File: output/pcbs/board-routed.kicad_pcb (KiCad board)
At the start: 2 copper layers, 141.8 x 108.1 mm, 41 parts

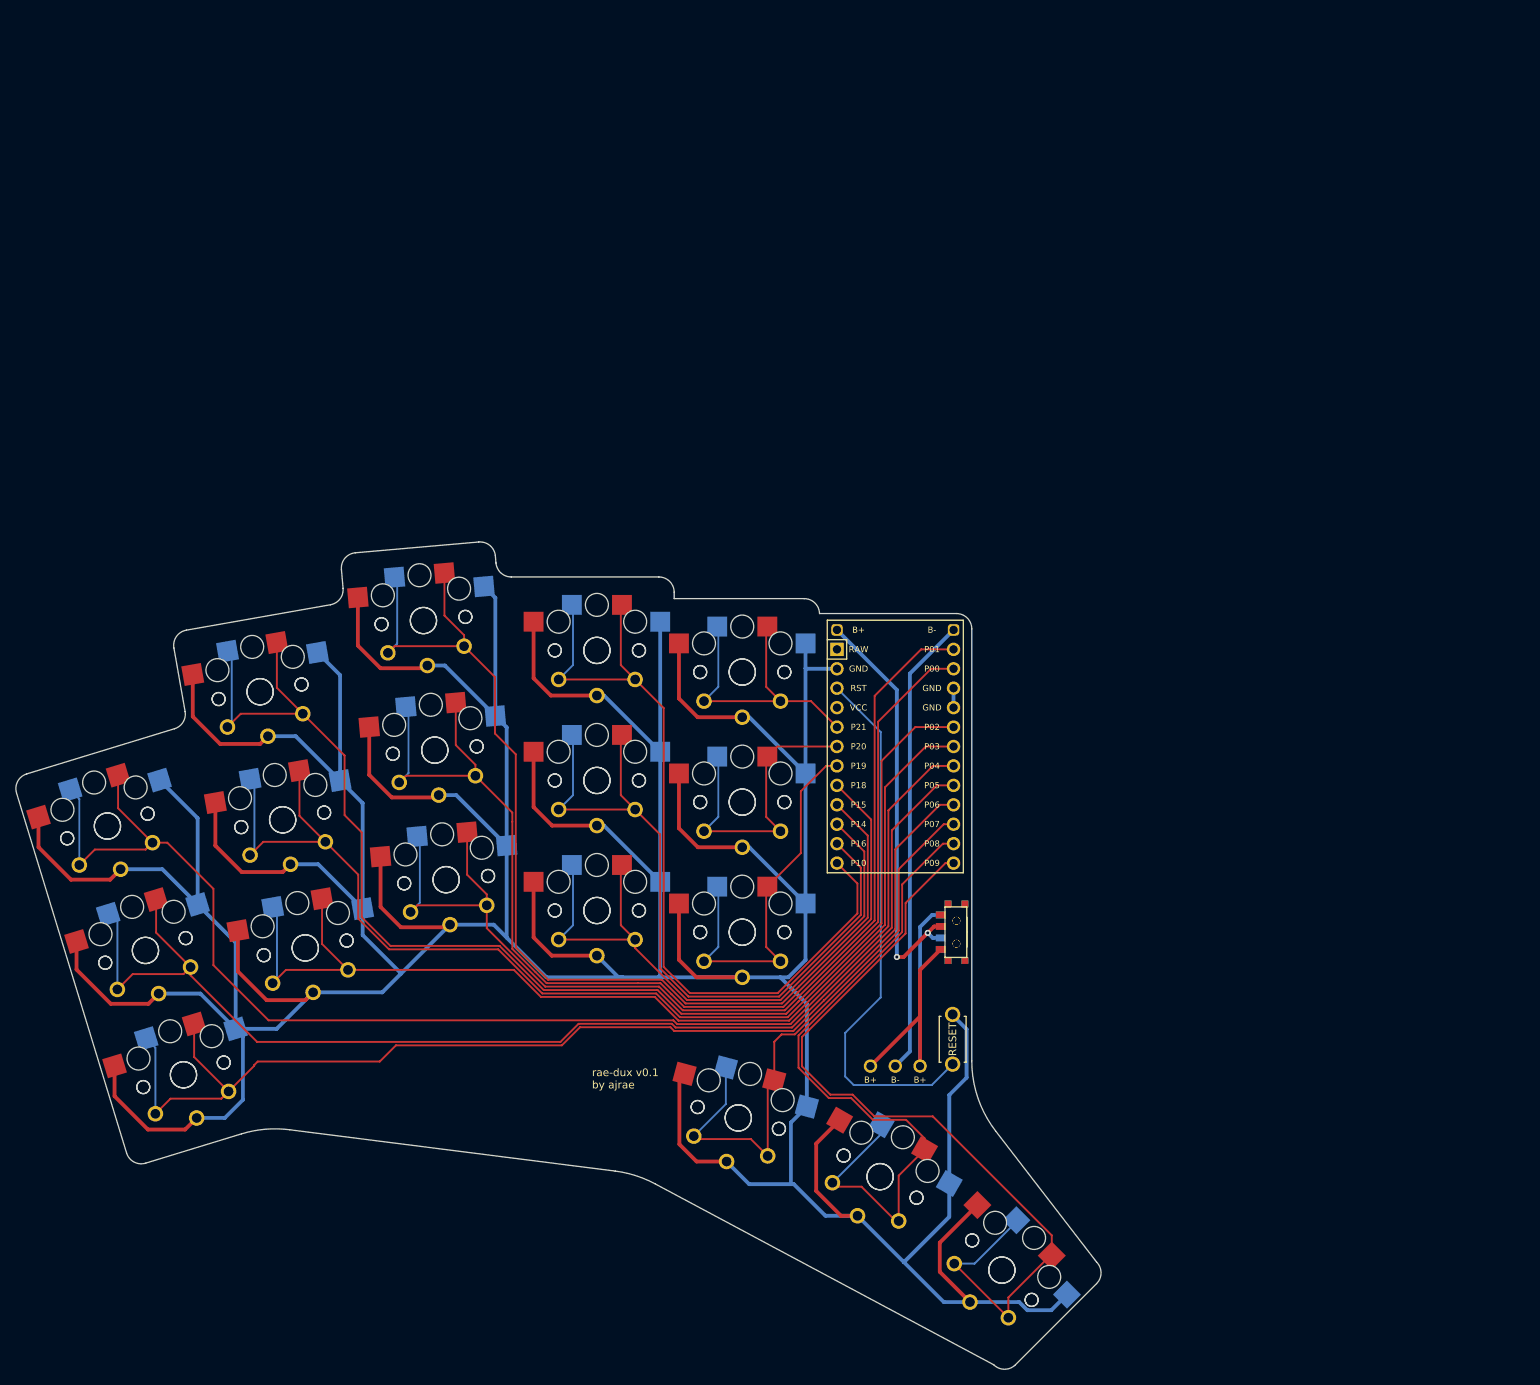
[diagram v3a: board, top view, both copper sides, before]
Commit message: Increasing pinky stagger and fixing battery footprint to actually work with JST PH (fixed upstream in ergogen fork).
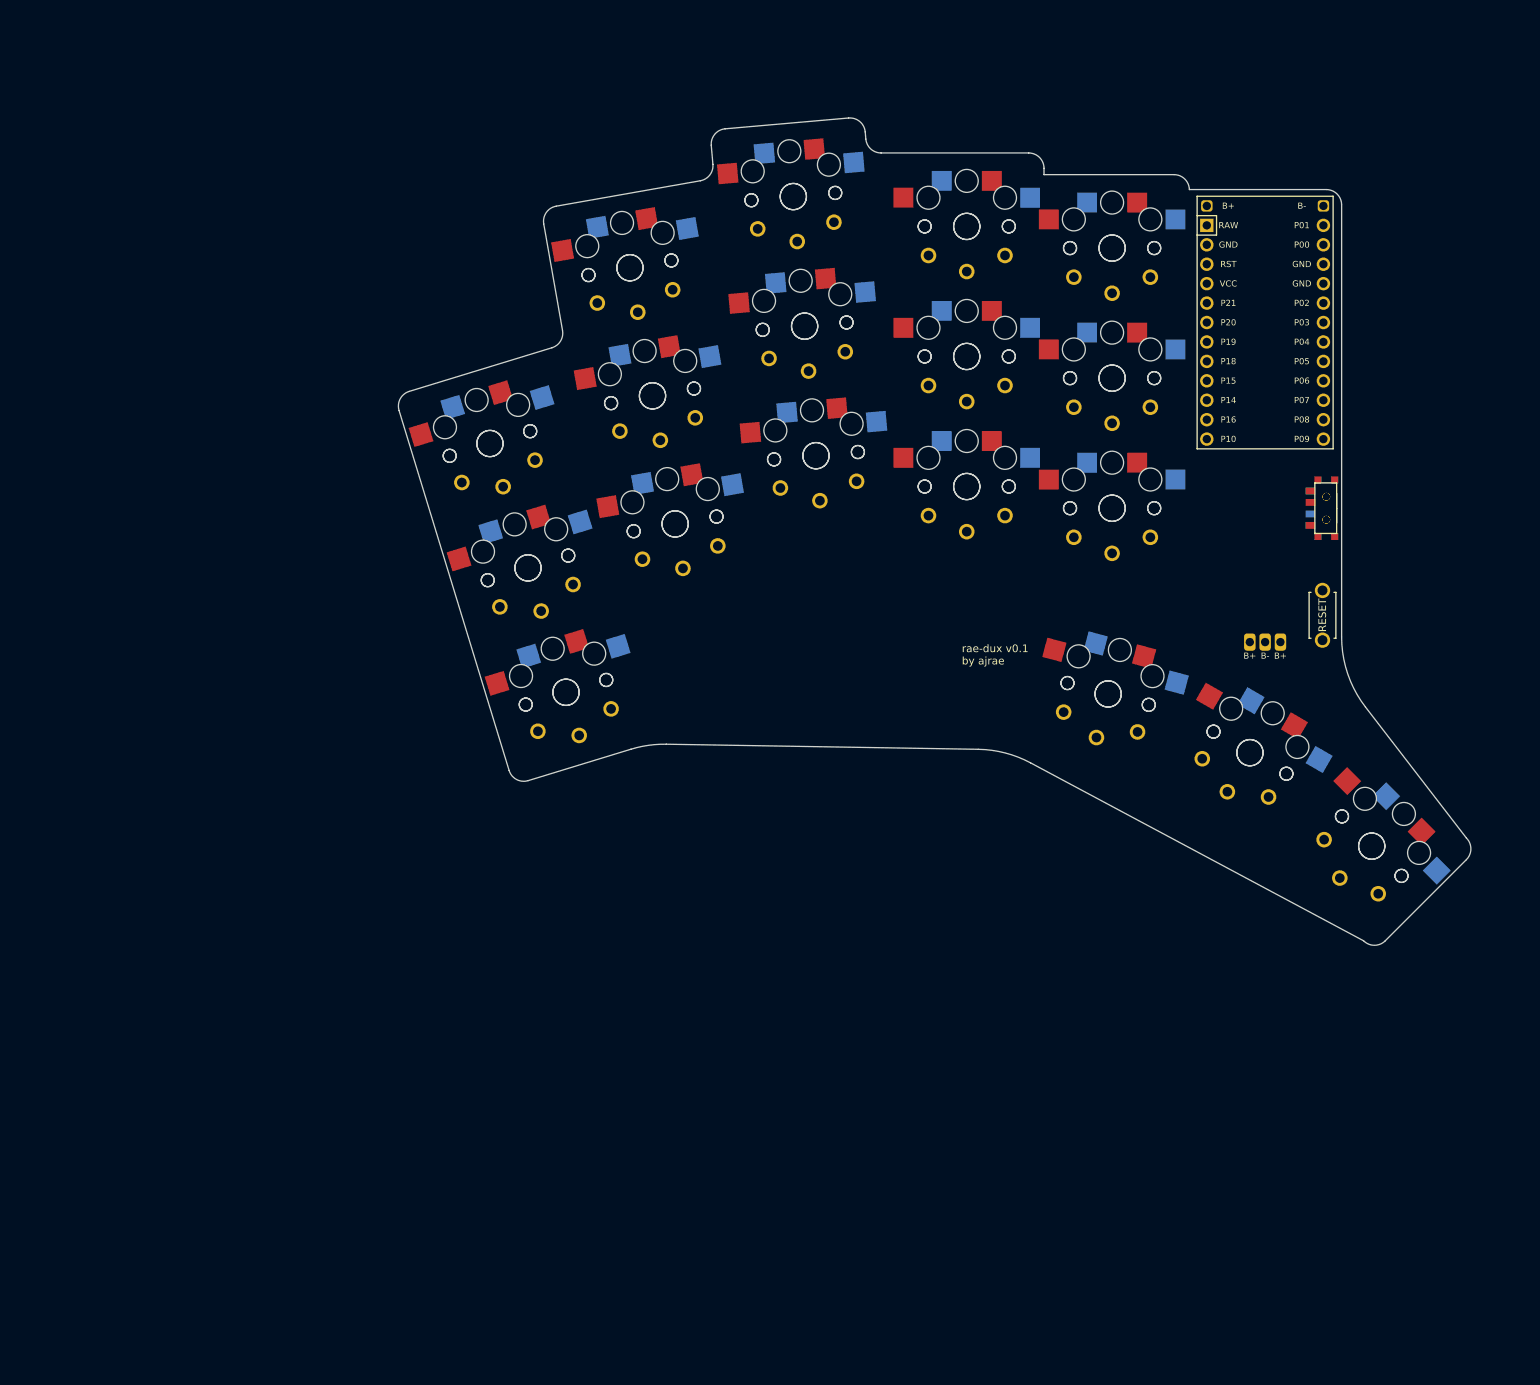
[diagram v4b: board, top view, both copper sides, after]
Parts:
- moved B1 73.5 mm to (161.9, -59.3)
- moved PAD1 73.5 mm to (154.4, -55.8)
- moved S17 73.5 mm to (92.7, -114.0)
- moved S18 73.5 mm to (92.7, -114.0)
- moved S25 73.5 mm to (134.4, -73.3)
- moved S26 73.5 mm to (134.4, -73.3)
- moved T1 73.5 mm to (162.4, -73.3)
- moved T2 73.5 mm to (162.4, -73.3)
- moved S35 73.5 mm to (168.3, -29.1)
- moved S36 73.5 mm to (168.3, -29.1)
- moved MCU1 73.5 mm to (154.4, -96.3)
- moved S10 73.5 mm to (74.3, -88.0)
- moved S11 73.5 mm to (71.4, -104.7)
- moved S12 73.5 mm to (71.4, -104.7)
- moved S27 73.5 mm to (134.4, -90.3)
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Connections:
- MCU1 pad 25: Bplus -> Bminus
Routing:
- net GND: track 867.7 -> 0.00 mm
- net P0: track 178.0 -> 0.00 mm
- net P4: track 175.0 -> 0.00 mm
- net P5: track 158.3 -> 0.00 mm
- net P2: track 154.8 -> 0.00 mm
- net P6: track 148.6 -> 0.00 mm
- net P15: track 143.7 -> 0.00 mm
- net P3: track 138.9 -> 0.00 mm
- net P1: track 136.7 -> 0.00 mm
- net P18: track 130.3 -> 0.00 mm
- net P9: track 111.0 -> 0.00 mm
- net P10: track 109.0 -> 0.00 mm
- net P16: track 96.1 -> 0.00 mm
- net P8: track 92.0 -> 0.00 mm
- net P14: track 83.1 -> 0.00 mm
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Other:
- board size 141.8 x 108.1 mm -> 140.2 x 108.1 mm

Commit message: Finished routing the latest revision.
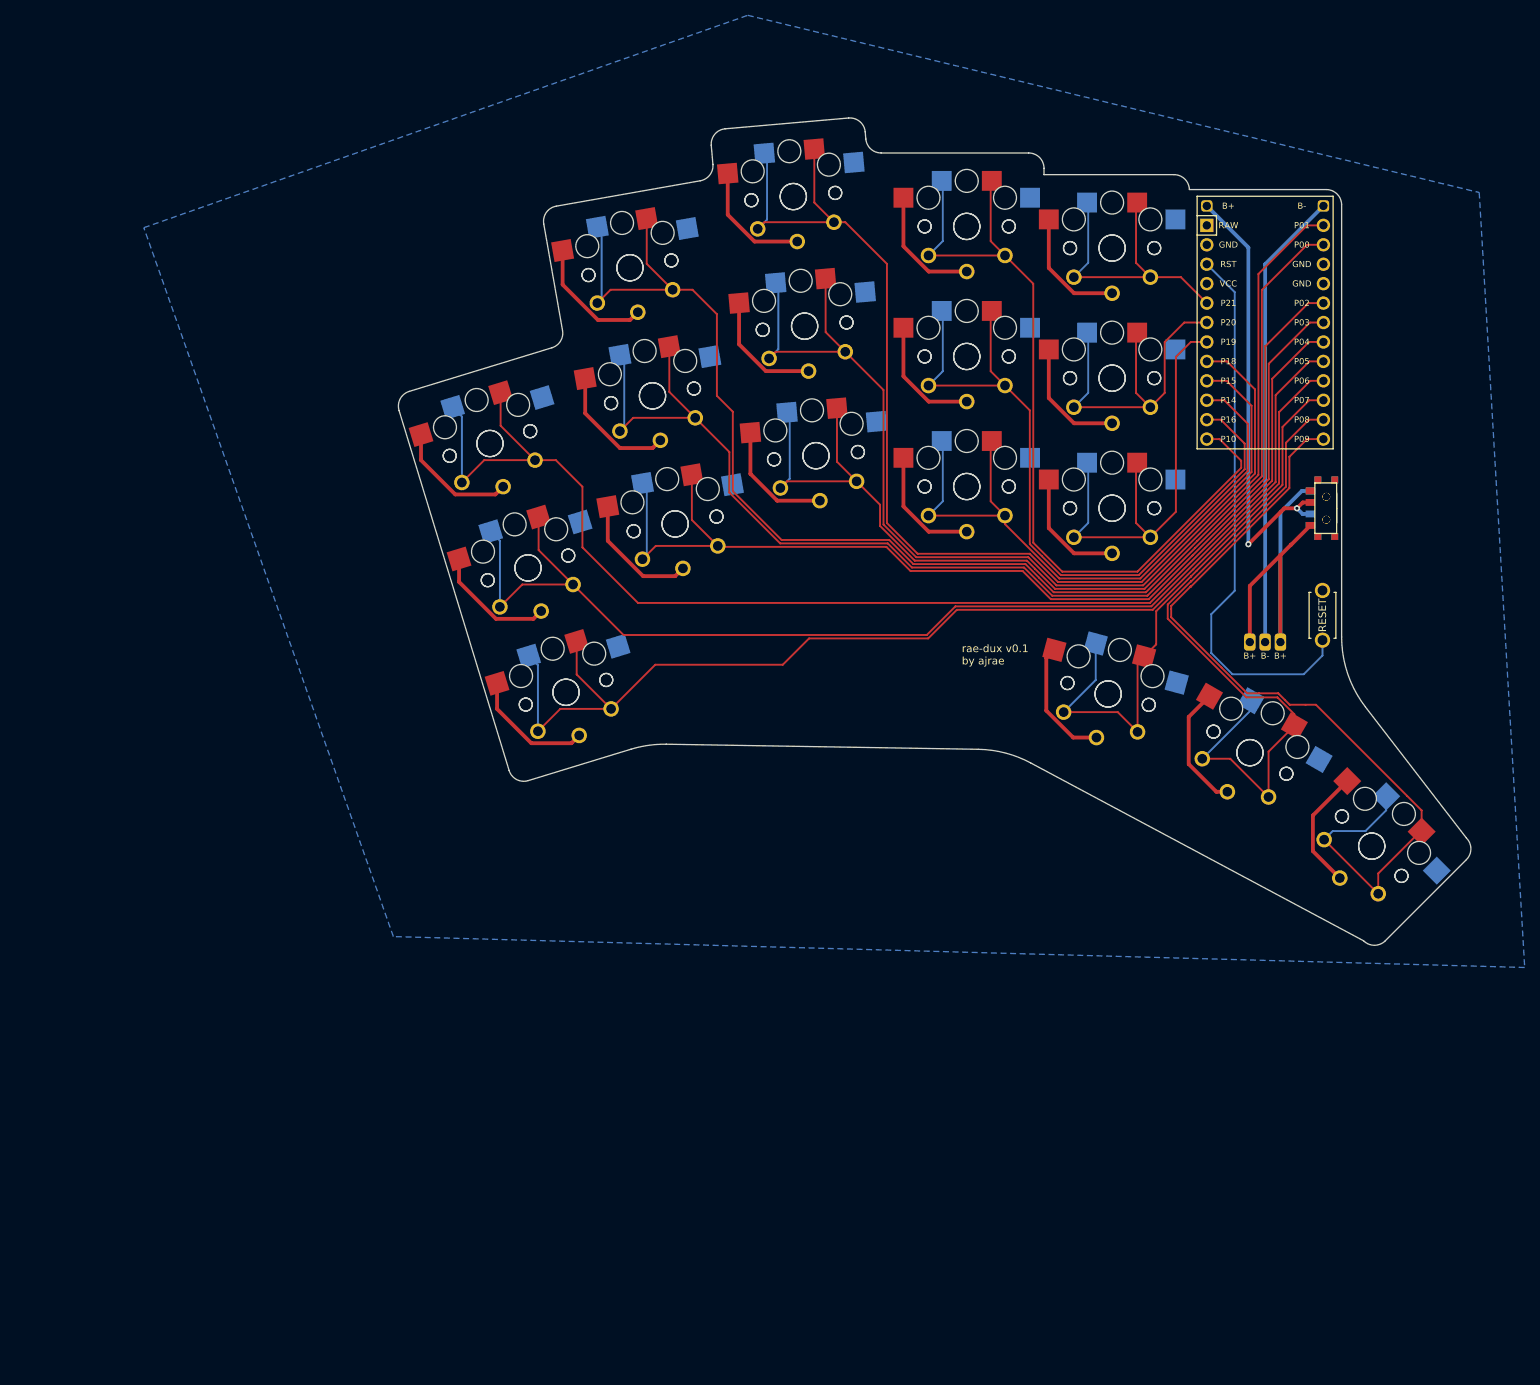
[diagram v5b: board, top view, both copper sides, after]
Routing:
- net GND: track 0.00 -> 291.4 mm
- net P0: track 0.00 -> 178.5 mm
- net P4: track 0.00 -> 169.1 mm
- net P5: track 0.00 -> 154.1 mm
- net P2: track 0.00 -> 152.4 mm
- net P6: track 0.00 -> 148.1 mm
- net P15: track 0.00 -> 147.2 mm
- net P3: track 0.00 -> 137.5 mm
- net P1: track 0.00 -> 135.0 mm
- net P18: track 0.00 -> 132.8 mm
- net P10: track 0.00 -> 111.2 mm
- net P9: track 0.00 -> 110.9 mm
- net P16: track 0.00 -> 98.3 mm
- net P8: track 0.00 -> 90.5 mm
- net P14: track 0.00 -> 85.6 mm
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- added copper zone on B.Cu, net GND
